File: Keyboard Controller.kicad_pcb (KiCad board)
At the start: 2 copper layers, 76.2 x 101.6 mm, 52 parts, among them SW1 SW_Push, SW2 SW_Push, SW3 SW_Push, SW4 SW_Push, SW5 SW_Push, SW6 SW_Push, SW7 SW_Push, SW8 SW_Push, SW9 SW_Push, U1 Teensy-3.2

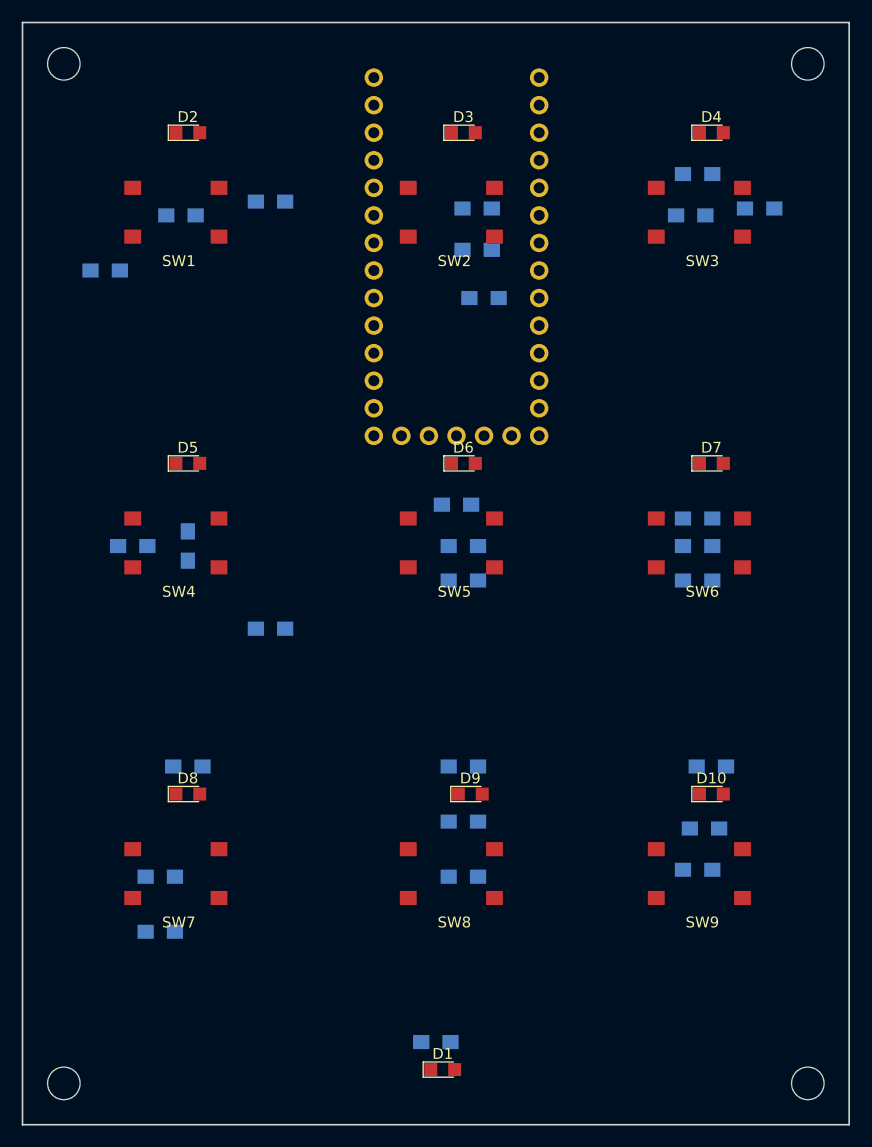
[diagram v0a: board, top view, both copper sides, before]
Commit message: Changed pinout for easier layout
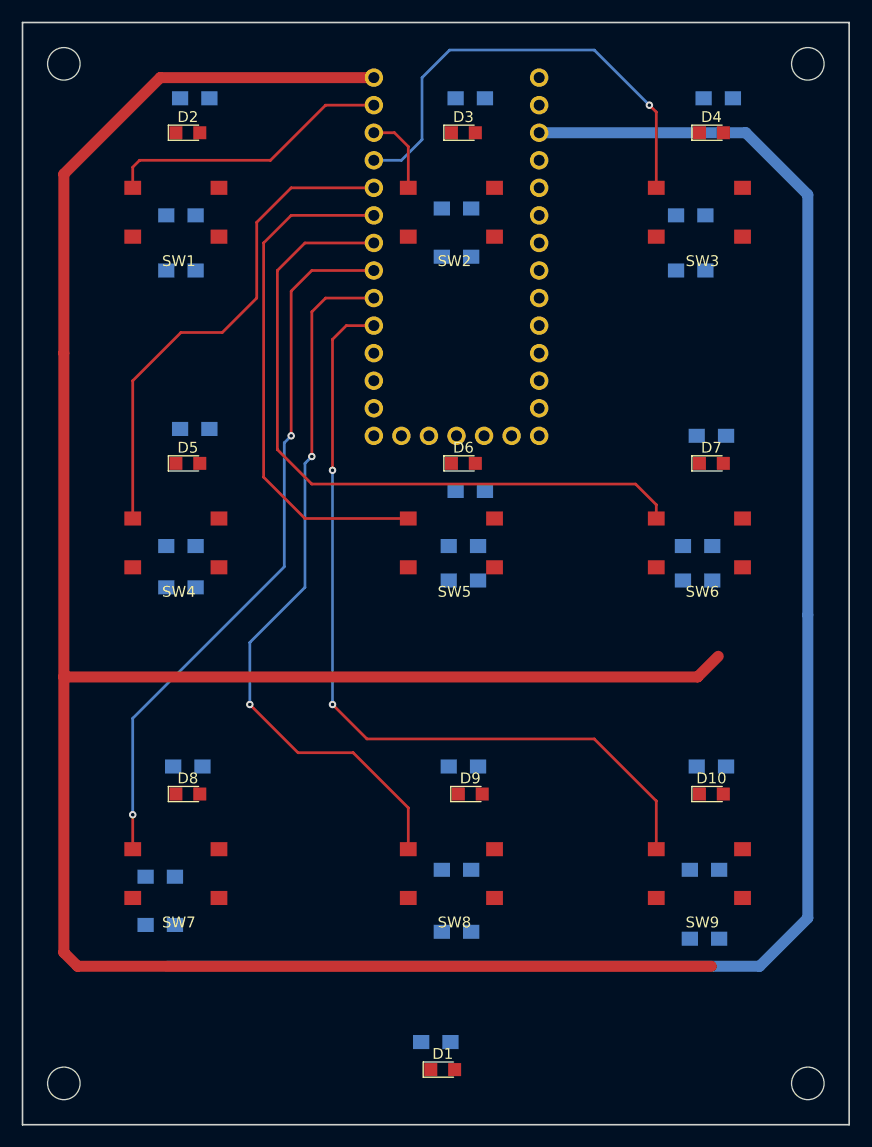
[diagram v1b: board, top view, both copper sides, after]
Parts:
- moved R5 19.7 mm to (112.4, 78.1)
- moved R3 18.5 mm to (137.8, 47.6)
- moved R2 11.8 mm to (112.4, 47.6)
- moved R26 10.2 mm to (136.5, 124.5)
- moved R16 8.54 mm to (158.1, 63.5)
- moved R7 7.73 mm to (160.0, 78.7)
- moved R4 7.24 mm to (160.7, 47.6)
- moved R12 6.98 mm to (111.1, 63.5)
- moved R27 6.38 mm to (159.4, 125.1)
- moved R17 4.44 mm to (111.1, 88.9), turned to 180 degrees
- moved R18 3.86 mm to (111.1, 92.7), turned to 0 degrees
- moved R28 3.81 mm to (159.4, 118.7), turned to 180 degrees
- moved R14 2.01 mm to (136.5, 62.2)
- moved R13 1.91 mm to (136.5, 57.8), turned to 180 degrees
- moved R6 1.80 mm to (137.8, 83.8)
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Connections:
- net Net-(SW1-Pad1) renamed /SW1
- net Net-(SW2-Pad1) renamed /SW2
- net Net-(SW3-Pad1) renamed /SW3
- net Net-(SW4-Pad1) renamed /SW4
- net Net-(SW5-Pad1) renamed /SW5
- net Net-(SW6-Pad1) renamed /SW6
- net Net-(SW7-Pad1) renamed /SW7
- net Net-(SW8-Pad1) renamed /SW8
- net Net-(SW9-Pad1) renamed /SW9
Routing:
- net GND: track 0.00 -> 225.3 mm
- net +3V3: track 0.00 -> 154.7 mm
- net /SW9: track 0.00 -> 76.0 mm, vias 0 -> 2
- net /SW8: track 0.00 -> 67.2 mm, vias 0 -> 2
- net /SW7: track 0.00 -> 65.9 mm, vias 0 -> 2
- net /SW6: track 0.00 -> 64.8 mm
- net /SW5: track 0.00 -> 47.7 mm
- net /SW4: track 0.00 -> 46.4 mm
- net /SW3: track 0.00 -> 42.9 mm, vias 0 -> 1
- net /SW1: track 0.00 -> 26.5 mm
- net /SW2: track 0.00 -> 7.51 mm
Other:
- net class Default: clearance 0.2 -> 0.1524; trace_width 0.25 -> 0.254; via_dia 0.6 -> 0.6858; via_drill 0.4 -> 0.3302
- rule trace_clearance: 0.2 -> 0.1524
- rule trace_min: 0.2 -> 0.1524
- rule via_min_drill: 0.3 -> 0.3302
- rule via_min_size: 0.4 -> 0.6858

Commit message: Moved all non power traces to top side
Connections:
- U1 pad 0: /SW1 -> /LED1
- U1 pad 1: /SW2 -> /SW1
- U1 pad 10: /LED2 -> Net-(U1-Pad10)
- U1 pad 11: /LED3 -> Net-(U1-Pad11)
- U1 pad 12: /LED4 -> Net-(U1-Pad12)
- U1 pad 13: /LED5 -> Net-(U1-Pad13)
- U1 pad 14: /LED6 -> Net-(U1-Pad14)
- U1 pad 15: /LED7 -> Net-(U1-Pad15)
- U1 pad 16: /LED8 -> /SW5
- U1 pad 17: /LED9 -> /LED5
- U1 pad 18: Net-(U1-Pad18) -> /SW8
- U1 pad 19: Net-(U1-Pad19) -> /LED8
- U1 pad 2: /SW3 -> /LED3
- U1 pad 20: Net-(U1-Pad20) -> /SW9
- U1 pad 21: Net-(U1-Pad21) -> /LED9
- U1 pad 22: Net-(U1-Pad22) -> /SW6
- U1 pad 23: Net-(U1-Pad23) -> /LED6
- U1 pad 3: /SW4 -> /SW3
- U1 pad 4: /SW5 -> /LED2
- U1 pad 5: /SW6 -> /SW2
- U1 pad 6: /SW7 -> /LED4
- U1 pad 7: /SW8 -> /SW4
- U1 pad 8: /SW9 -> /LED7
- U1 pad 9: /LED1 -> /SW7
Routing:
- net GND: track 225.3 -> 0.00 mm
- net +3V3: track 154.7 -> 0.00 mm
- net /LED8: track 0.00 -> 67.0 mm, vias 0 -> 1
- net /LED9: track 0.00 -> 60.6 mm, vias 0 -> 1
- net /LED7: track 0.00 -> 52.6 mm, vias 0 -> 1
- net /LED3: track 0.00 -> 43.9 mm, vias 0 -> 1
- net /LED4: track 0.00 -> 36.4 mm, vias 0 -> 1
- net /LED6: track 0.00 -> 34.4 mm, vias 0 -> 1
- net /LED5: track 0.00 -> 30.1 mm, vias 0 -> 1
- net /SW6: track 64.8 -> 38.5 mm
- net /LED2: track 0.00 -> 17.2 mm
- net /LED1: track 0.00 -> 15.5 mm, vias 0 -> 1
- net /SW5: track 47.7 -> 33.1 mm
- net /SW9: track 76.0 -> 61.8 mm, vias 2 -> 0
- net /SW4: track 46.4 -> 35.8 mm
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
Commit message: Finished preliminary layout
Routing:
- net +3V3: track 0.00 -> 21.7 mm, vias 0 -> 9
- net Net-(R25-Pad2): track 0.00 -> 11.2 mm, vias 0 -> 1
- net Net-(R23-Pad2): track 0.00 -> 10.7 mm, vias 0 -> 1
- net Net-(R15-Pad2): track 0.00 -> 10.1 mm, vias 0 -> 1
- net Net-(R27-Pad1): track 0.00 -> 9.68 mm, vias 0 -> 1
- net Net-(R17-Pad2): track 0.00 -> 8.61 mm, vias 0 -> 1
- net Net-(R19-Pad2): track 0.00 -> 8.27 mm, vias 0 -> 1
- net Net-(R11-Pad2): track 0.00 -> 8.15 mm, vias 0 -> 1
- net Net-(R13-Pad2): track 0.00 -> 7.63 mm, vias 0 -> 1
- net Net-(R21-Pad2): track 0.00 -> 7.59 mm, vias 0 -> 1
- net Net-(D1-Pad1): track 0.00 -> 6.91 mm, vias 0 -> 1
- net Net-(D10-Pad1): track 0.00 -> 5.25 mm, vias 0 -> 1
- net Net-(D6-Pad1): track 0.00 -> 4.83 mm, vias 0 -> 1
- net Net-(D7-Pad1): track 0.00 -> 4.68 mm, vias 0 -> 1
- net Net-(D8-Pad1): track 0.00 -> 4.39 mm, vias 0 -> 1
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- added copper zone on F.Cu, net +3V3
- added copper zone on B.Cu, net GND

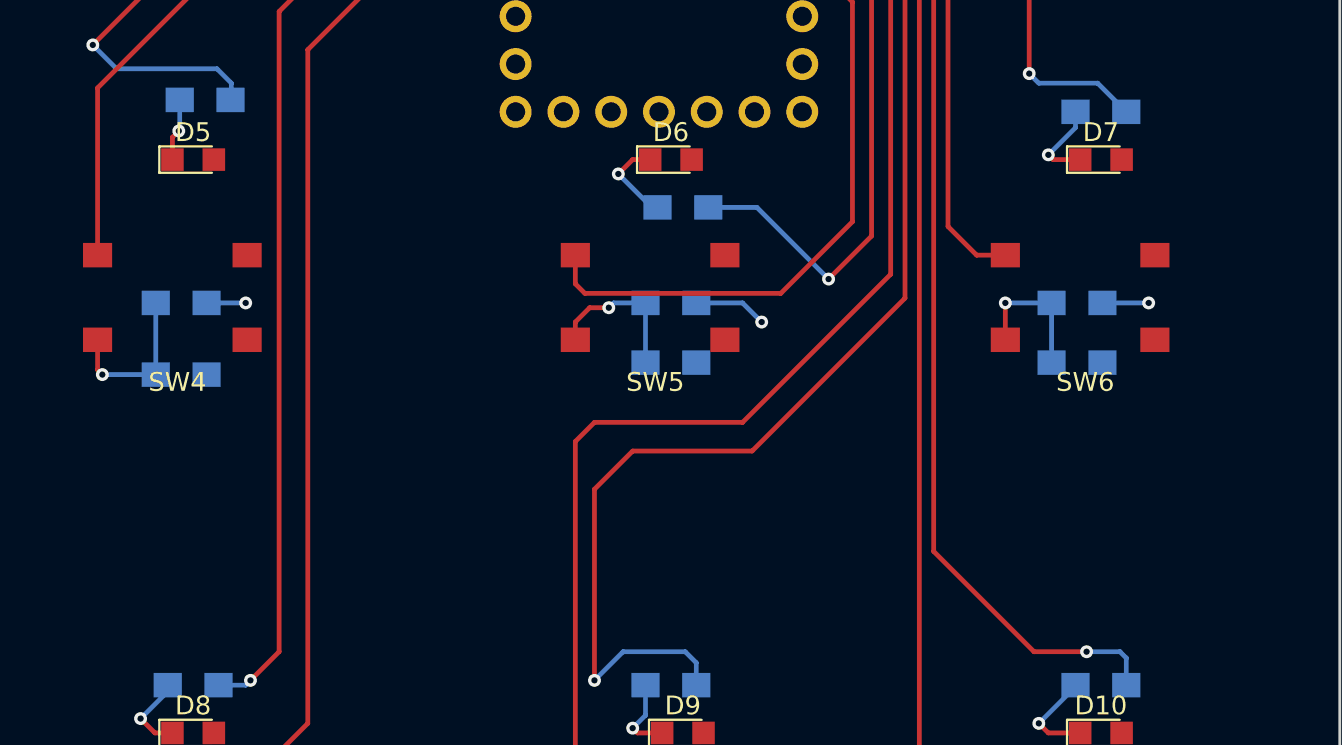
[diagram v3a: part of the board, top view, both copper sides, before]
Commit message: Moved silkscreen into place
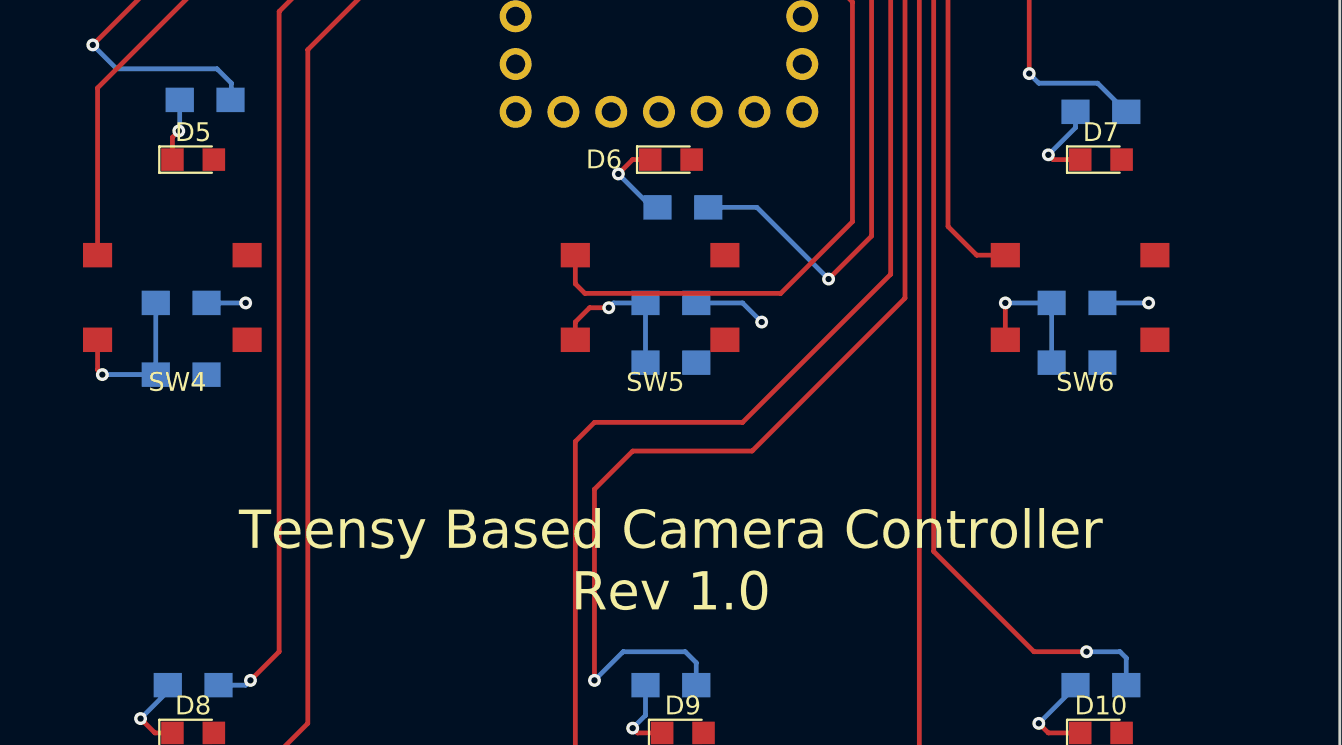
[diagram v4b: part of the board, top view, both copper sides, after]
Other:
- board text added: "Teensy Based Camera Controller Rev 1.0"
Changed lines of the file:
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@@
     (links 75)
     (no_connects 0)
-    (area 92.963314 39.5226 176.276686 143.4574)
+    (area 96.444999 40.564999 172.795001 142.315001)
     (thickness 1.6)
-    (drawings 4)
+    (drawings 5)
     (tracks 254)
     (zones 0)
@@
   (page A4)
   (layers
-    (0 F.Cu signal)
-    (31 B.Cu signal)
+    (0 F.Cu signal hide)
+    (31 B.Cu signal hide)
     (32 B.Adhes user)
     (33 F.Adhes user)
@@
     (aux_axis_origin 0 0)
     (grid_origin 100.33 52.07)
-    (visible_elements 7FFFFFFF)
+    (visible_elements 7FFEFFFF)
     (pcbplotparams
       (layerselection 0x00030_80000001)
@@
     (tags "LED led 0805 SMD smd SMT smt smdled SMDLED smtled SMTLED")
     (attr smd)
-    (fp_text reference D6 (at 0 -1.45) (layer F.SilkS)
+    (fp_text reference D6 (at -3.556 0) (layer F.SilkS)
       (effects (font (size 1 1) (thickness 0.15)))
     )
@@
     (tags "resistor 0805")
     (attr smd)
-    (fp_text reference R19 (at 0 2.1 180) (layer B.SilkS)
+    (fp_text reference R19 (at 4.318 0 180) (layer B.SilkS)
       (effects (font (size 1 1) (thickness 0.15)) (justify mirror))
     )
@@
   (module Key:Teensy-32 (layer B.Cu)
     (at 136.525 60.96 180)
-    (fp_text reference U1 (at 0 -2.54 180) (layer B.SilkS)
+    (fp_text reference U1 (at -10.287 -16.764 180) (layer B.SilkS)
       (effects (font (size 1 1) (thickness 0.15)) (justify mirror))
     )
@@
     (pad 1 np_thru_hole circle (at 0 0) (size 3 3) (drill 3) (layers *.Cu *.Mask))
   )
+  (gr_text "Teensy Based Camera Controller\nRev 1.0" (at 137.16 102.616) (layer F.SilkS)
+    (effects (font (size 2.032 2.032) (thickness 0.381)))
+  )
   (gr_line (start 172.72 40.64) (end 96.52 40.64) (angle 90) (layer Edge.Cuts) (width 0.15))
